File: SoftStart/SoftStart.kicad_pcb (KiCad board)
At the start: 2 copper layers, 88 x 56 mm, 33 parts, among them J1 LIVE, J10 LIVE, J11 Conn_01x02, J18 SW2, J19 SW2, J2 NEUTRAL, J3 SW1, J4 SW2, J5 NEUTRAL, J6 SWOUTPUT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

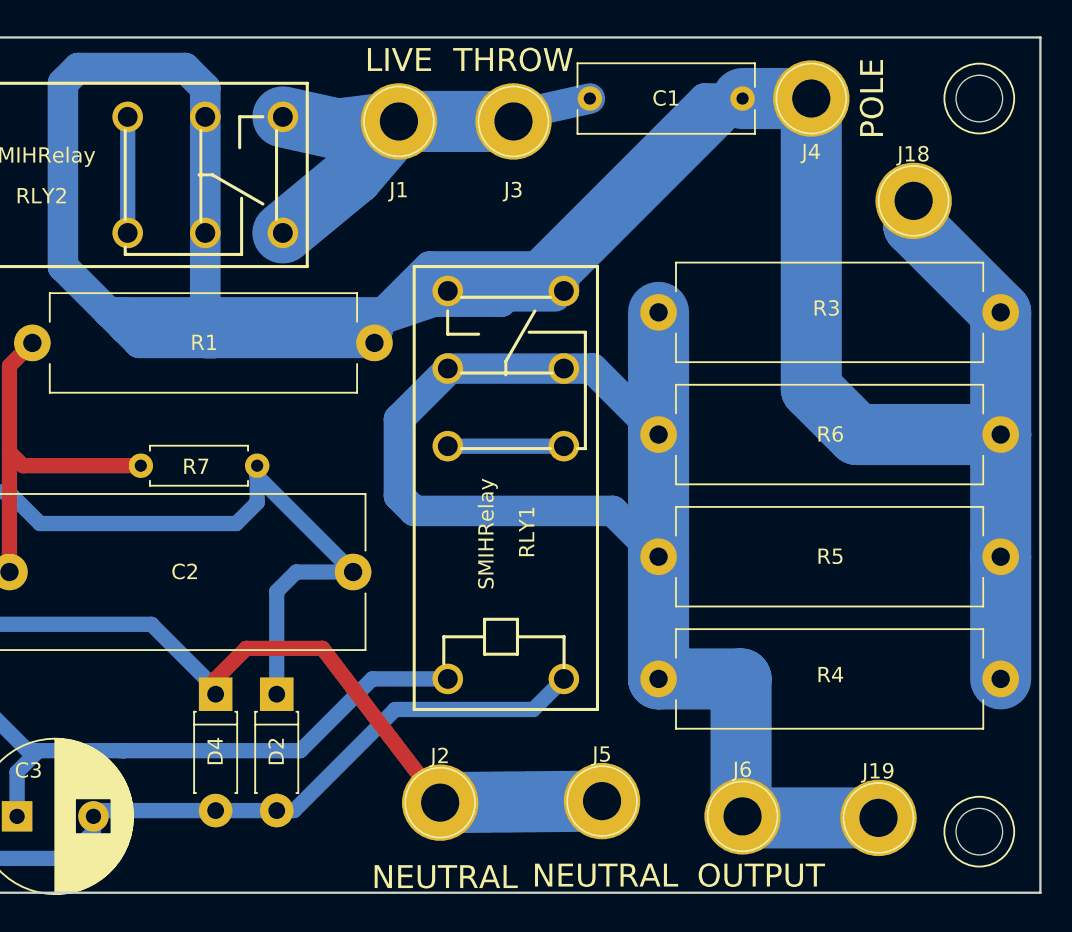
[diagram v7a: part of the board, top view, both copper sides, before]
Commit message: Additions of optional zener diodes to limit current surges
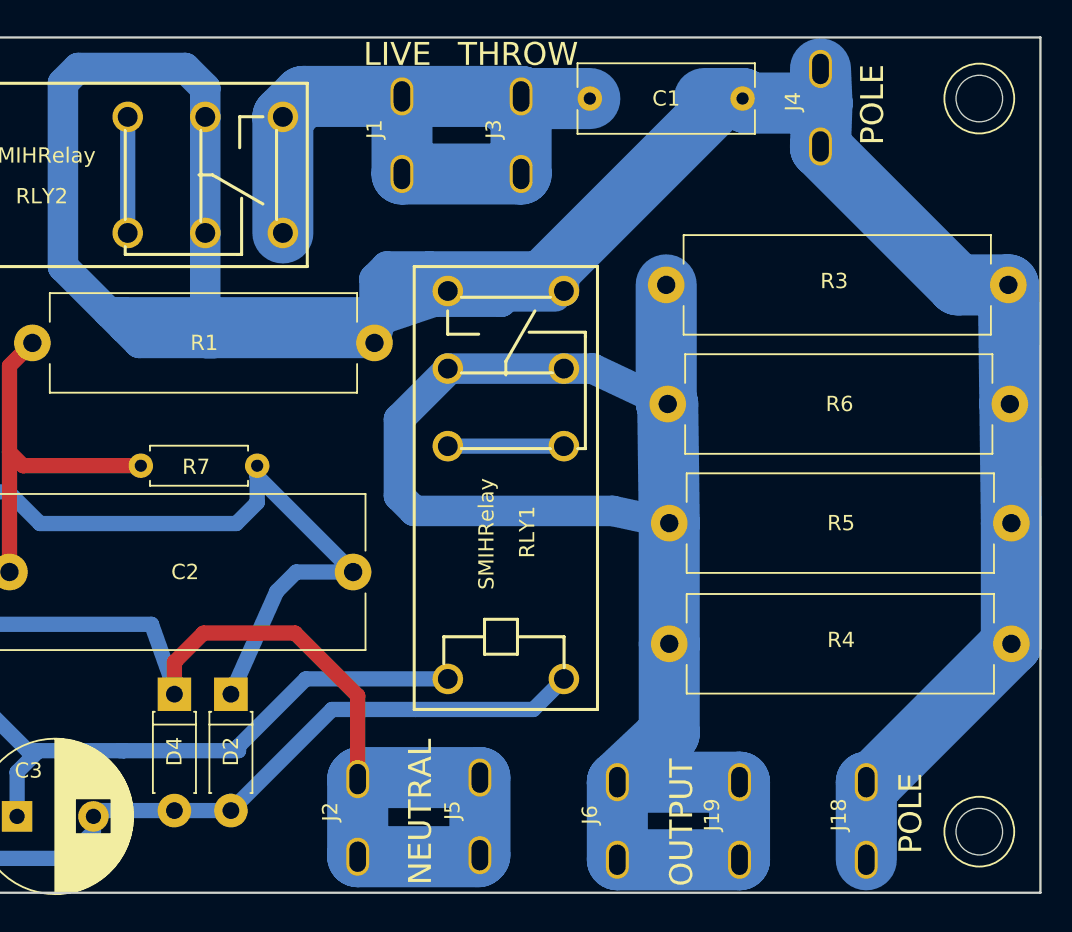
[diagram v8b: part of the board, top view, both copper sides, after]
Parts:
- J1, J18, J19, J2, J3, J4, J5, J6: footprint Connectors:1pin -> SoftStart:SpadeTerminal635
- moved J18 40.7 mm to (196.6, 120.3), turned to 90 degrees
- moved J19 9.10 mm to (188.3, 120.3), turned to 90 degrees
- moved J6 8.21 mm to (180.3, 120.3), turned to 90 degrees
- moved J5 8.06 mm to (171.3, 120.0), turned to 90 degrees
- moved J2 5.49 mm to (163.3, 120.1), turned to 90 degrees
- moved D2 3.00 mm to (155.0, 112.0)
- moved D4 2.70 mm to (151.3, 112.0)
- moved R4 2.40 mm to (183.7, 108.7)
- moved R5 2.31 mm to (183.7, 100.8)
- moved R6 2.09 mm to (183.6, 93.0)
- moved R3 1.87 mm to (183.5, 85.2)
- moved J3 1.03 mm to (174.0, 75.4), turned to 90 degrees
- moved J1 0.92 mm to (166.2, 75.4), turned to 90 degrees
- moved J4 0.85 mm to (193.6, 73.6), turned to 90 degrees
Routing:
- net Net-(C1-Pad2): track 31.1 -> 47.3 mm
- net Net-(D3-Pad2): track 56.4 -> 71.1 mm
- net Net-(J19-Pad1): track 91.2 -> 103.0 mm
- net Net-(C1-Pad1): track 232.7 -> 234.5 mm
- net Net-(C2-Pad1): track 52.3 -> 52.9 mm
